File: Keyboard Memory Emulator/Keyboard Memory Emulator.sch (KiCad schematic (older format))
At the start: 38 parts, among them J1 Conn_01x05, J2 Conn_01x01_Male, J3 Conn_01x02, J4 Conn_01x03, J5 Conn_01x02, J6 Conn_01x04, J7 Conn_01x05, J8 Conn_02x05_Odd_Even, SW1 PTS636 SL43 LFS, U1 UPD4168C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

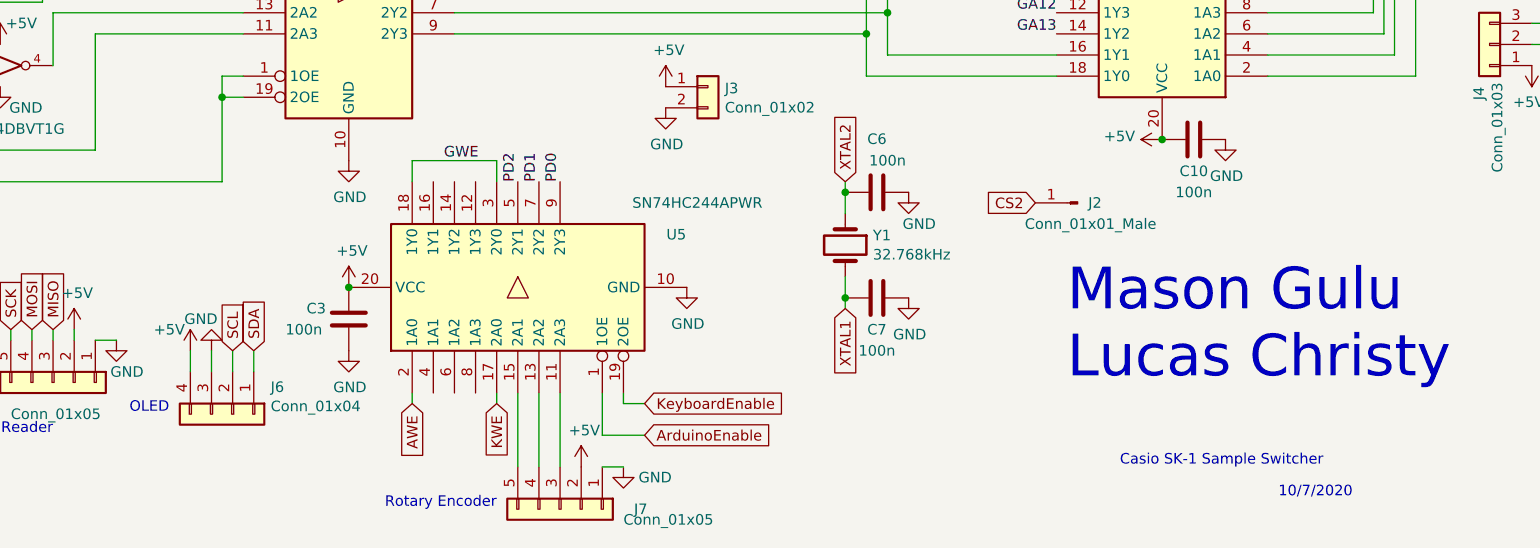
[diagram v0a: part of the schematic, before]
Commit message: Getting closer to finalization
With this update I believe it should be ready to order, waiting to get it looked over beforehand
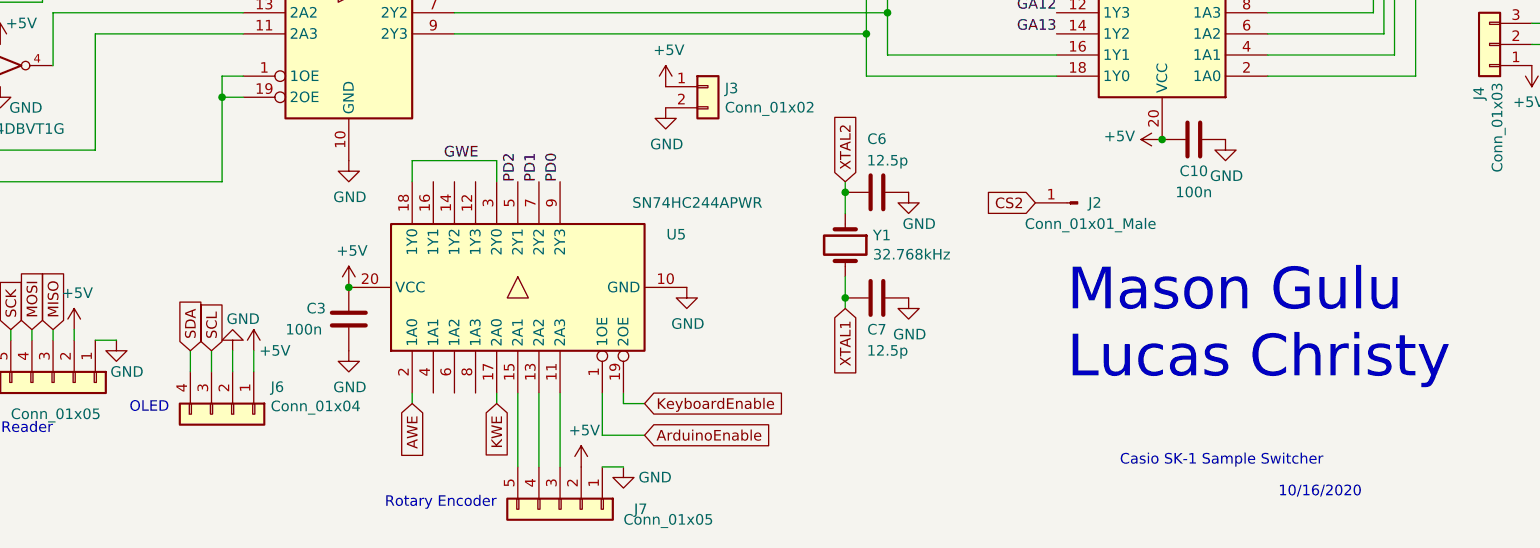
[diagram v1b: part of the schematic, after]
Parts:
- C6, C7: value 100n -> 12.5p
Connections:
- net +5V: now also J6.1 (Pin_1); no longer J6.4 (Pin_4)
- net GND: now also J6.2 (Pin_2); no longer J6.3 (Pin_3)
- net SCL: now also J6.3 (Pin_3); no longer J6.2 (Pin_2)
- net SDA: now also J6.4 (Pin_4); no longer J6.1 (Pin_1)
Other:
- note added: "10/16/2020"
- note removed: "10/7/2020"
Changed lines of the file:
@@
 Casio SK-1 Sample Switcher\n
 Text Notes 8150 7650 0    50   ~ 0
-10/7/2020
+10/16/2020
 Text GLabel 3250 2200 0    50   Input ~ 0
 KeyboardEnable
@@
 	0    1    1    0
 $EndComp
-Text GLabel 3300 6950 1    50   Input ~ 0
+Text GLabel 3000 6950 1    50   Input ~ 0
 SDA
-Text GLabel 3200 6950 1    50   Input ~ 0
+Text GLabel 3100 6950 1    50   Input ~ 0
 SCL
 $Comp
 L power:GND #PWR0136
 U 1 1 5F88AA9C
-P 3100 6950
-F 0 "#PWR0136" H 3100 6700 50  0001 C CNN
+P 3200 6950
+F 0 "#PWR0136" H 3200 6700 50  0001 C CNN
 F 1 "GND" H 3150 6800 50  0000 C CNN
-F 2 "" H 3100 6950 50  0001 C CNN
-F 3 "" H 3100 6950 50  0001 C CNN
-	1    3100 6950
+F 2 "" H 3200 6950 50  0001 C CNN
+F 3 "" H 3200 6950 50  0001 C CNN
+	1    3200 6950
 	-1   0    0    1
 $EndComp
@@
 L power:+5V #PWR0137
 U 1 1 5F88B7D3
-P 3000 6950
-F 0 "#PWR0137" H 3000 6800 50  0001 C CNN
-F 1 "+5V" H 2900 7050 50  0000 C CNN
-F 2 "" H 3000 6950 50  0001 C CNN
-F 3 "" H 3000 6950 50  0001 C CNN
-	1    3000 6950
+P 3300 6950
+F 0 "#PWR0137" H 3300 6800 50  0001 C CNN
+F 1 "+5V" H 3400 6950 50  0000 C CNN
+F 2 "" H 3300 6950 50  0001 C CNN
+F 3 "" H 3300 6950 50  0001 C CNN
+	1    3300 6950
 	1    0    0    -1
 $EndComp
@@
 P 6250 6700
 F 0 "C7" V 6400 6700 50  0000 C CNN
-F 1 "100n" V 6500 6700 50  0000 C CNN
+F 1 "12.5p" V 6500 6750 50  0000 C CNN
 F 2 "Capacitor_THT:C_Disc_D5.1mm_W3.2mm_P5.00mm" H 6288 6550 50  0001 C CNN
 F 3 "~" H 6250 6700 50  0001 C CNN
@@
 P 6250 6200
 F 0 "C6" V 5998 6200 50  0000 C CNN
-F 1 "100n" V 6100 6250 50  0000 C CNN
+F 1 "12.5p" V 6100 6250 50  0000 C CNN
 F 2 "Capacitor_THT:C_Disc_D5.1mm_W3.2mm_P5.00mm" H 6288 6050 50  0001 C CNN
 F 3 "~" H 6250 6200 50  0001 C CNN

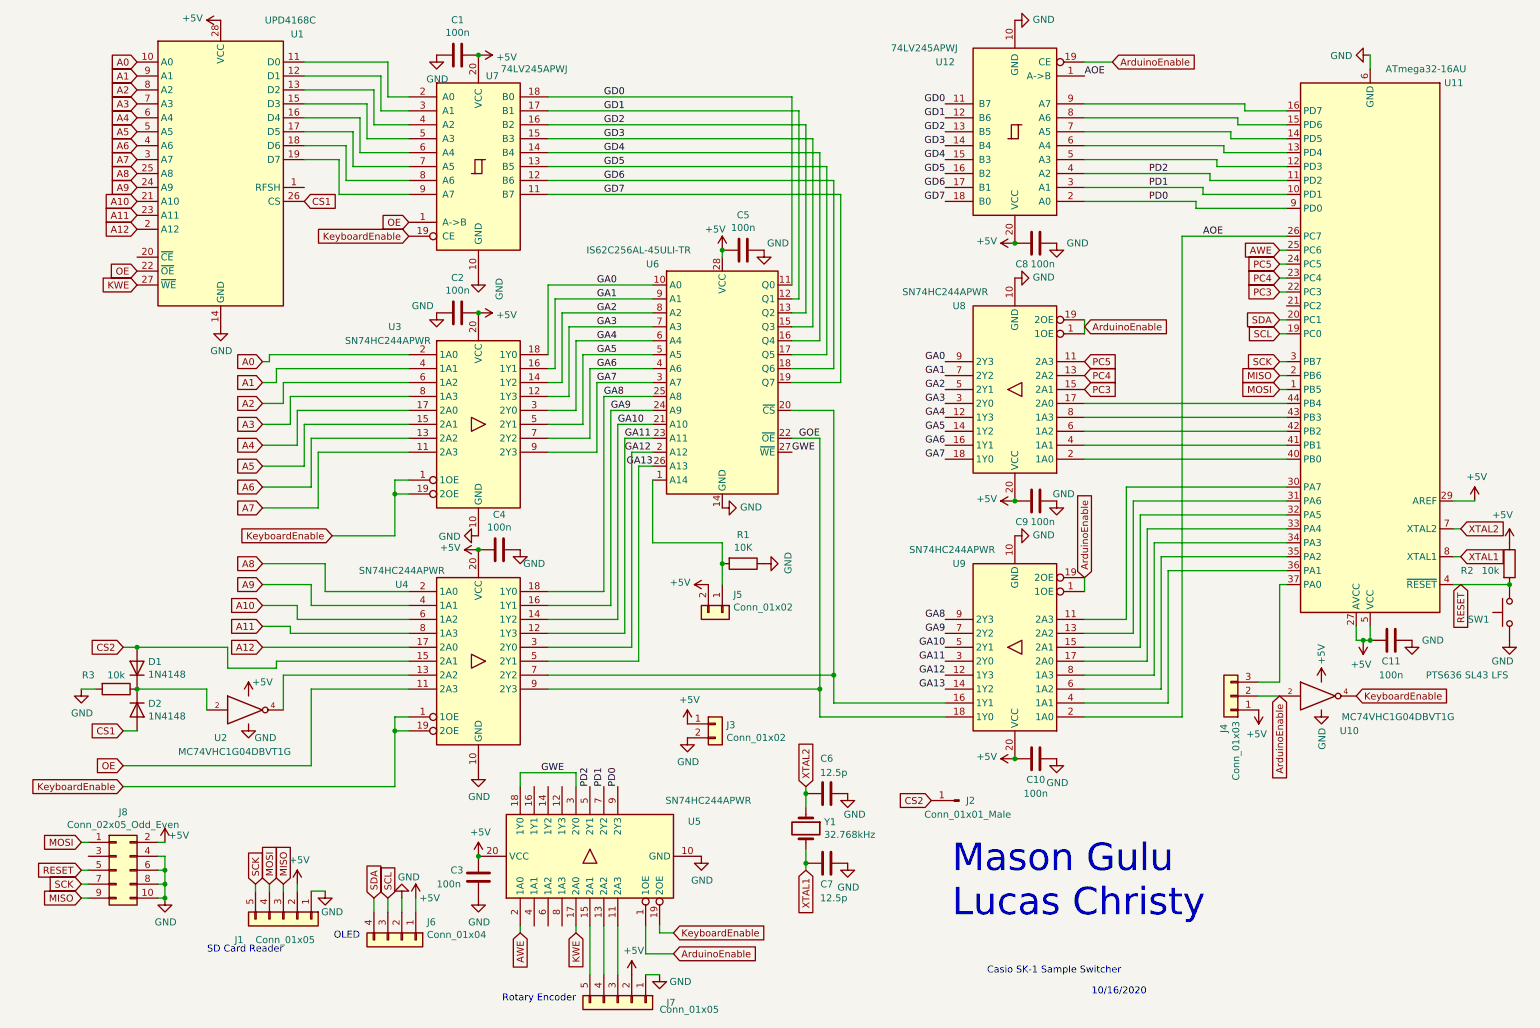
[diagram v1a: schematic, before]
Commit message: Schematic Restructuring to make it cleaner and easier to read. No actual changes as of yet, but planning to add some pull-up resistors on the I2C data bus.
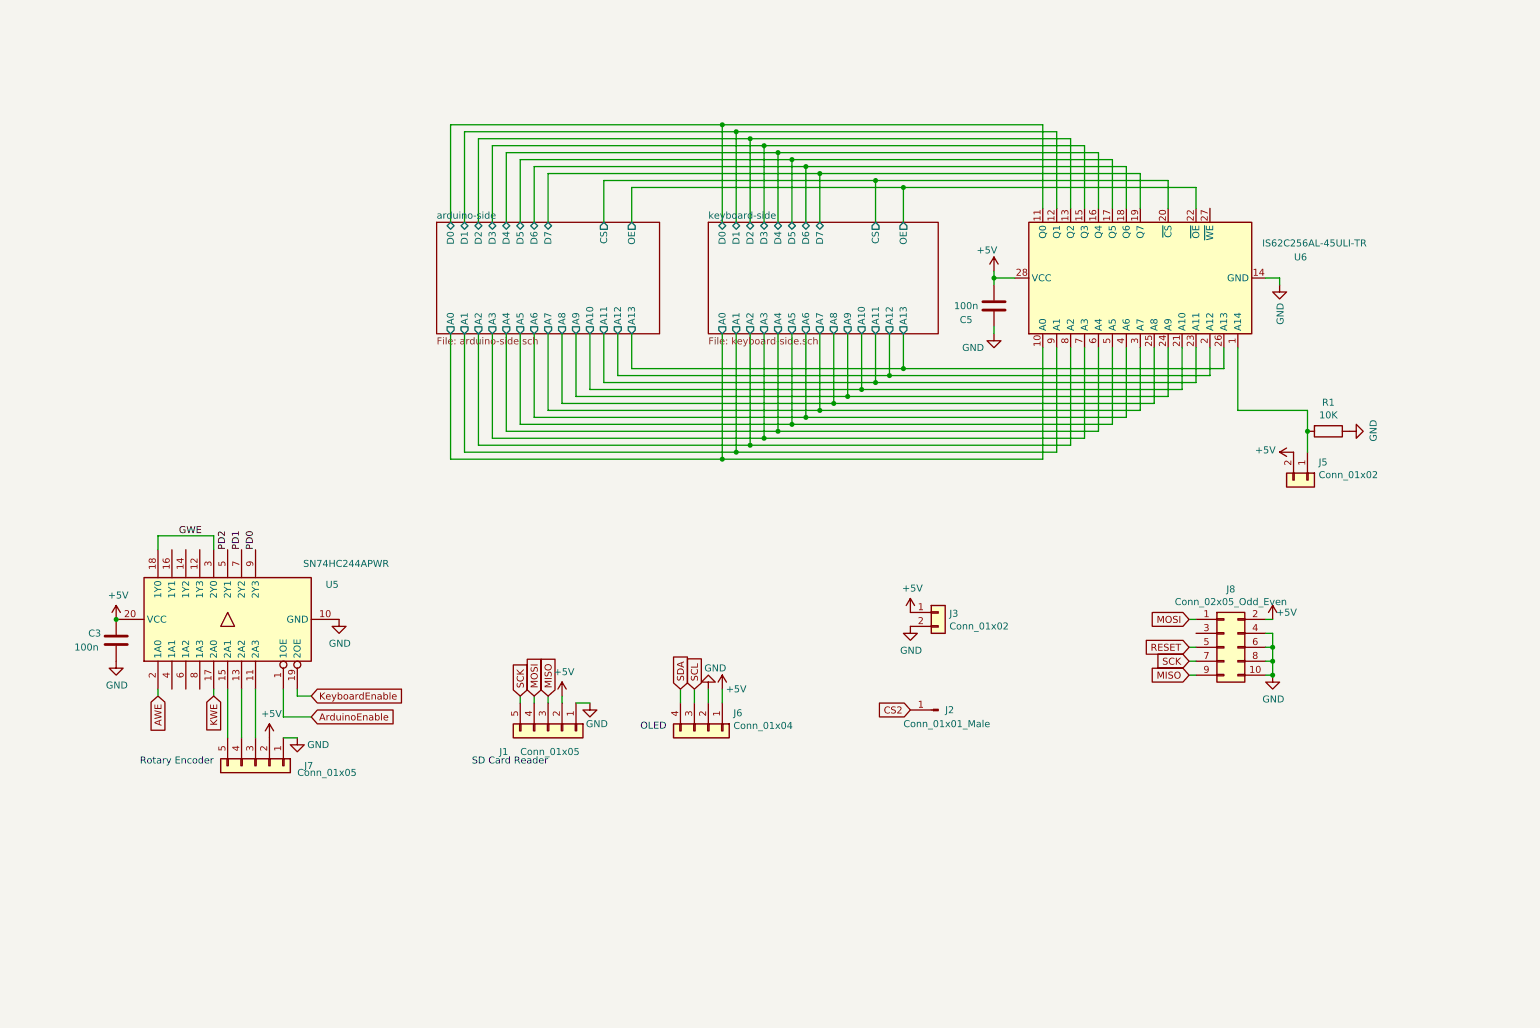
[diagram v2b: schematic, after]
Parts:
- removed C1, C10, C11, C2, C4, C8, C9: 100n, Capacitor_THT:C_Disc_D5.1mm_W3.2mm_P5.00mm, symbol Device:C
- removed C6, C7: 12.5p, Capacitor_THT:C_Disc_D5.1mm_W3.2mm_P5.00mm, symbol Device:C
- removed D1, D2: 1N4148, Diode_THT:D_DO-34_SOD68_P7.62mm_Horizontal, symbol Device:D
- removed J4: Conn_01x03, Connector_PinHeader_2.54mm:PinHeader_1x03_P2.54mm_Vertical, symbol Connector_Generic:Conn_01x03
- removed R2, R3: 10k, Resistor_THT:R_Axial_DIN0204_L3.6mm_D1.6mm_P5.08mm_Horizontal, symbol Device:R
- removed SW1: PTS636 SL43 LFS, Button_Switch_SMD:SW_SPST_REED_CT05-XXXX-G1, symbol Switch:SW_Push
- removed U1: UPD4168C, Package_DIP:DIP-28_W15.24mm, symbol myramchip:UPD4168C
- removed U10, U2: MC74VHC1G04DBVT1G, Package_SO:thispackagefucker, symbol 74xGxx:74AHC1G04
- removed U11: ATmega32-16AU, Package_QFP:TQFP-44_10x10mm_P0.8mm, symbol MCU_Microchip_ATmega:ATmega32-16AU
- removed U12, U7: 74LV245APWJ, Package_SO:TSSOP-20_4.4x6.5mm_P0.65mm, symbol 74xx:74LS245
- removed U3, U4, U8, U9: SN74HC244APWR, Package_SO:TSSOP-20_4.4x6.5mm_P0.65mm, symbol 74xx:74HC244
- removed Y1: 32.768kHz, Crystal:Crystal_C26-LF_D2.1mm_L6.5mm_Horizontal, symbol Device:Crystal
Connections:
- net GWE: no longer U6.27 (~WE)
- net arduino-side/A12: now reaches U6.2 (A12)
- net arduino-side/CS: now reaches U6.20 (~CS)
- net GA0 renamed arduino-side/A0
- net GA1 renamed arduino-side/A1
- net GA10 renamed arduino-side/A10
- net GA11 renamed arduino-side/A11
- net GA13 renamed arduino-side/A13
- net GA2 renamed arduino-side/A2
- net GA3 renamed arduino-side/A3
- net GA4 renamed arduino-side/A4
- net GA5 renamed arduino-side/A5
- net GA6 renamed arduino-side/A6
- net GA7 renamed arduino-side/A7
- net GA8 renamed arduino-side/A8
- net GA9 renamed arduino-side/A9
- net GD0 renamed arduino-side/D0
- net GD1 renamed arduino-side/D1
- net GD2 renamed arduino-side/D2
- net GD3 renamed arduino-side/D3
- net GD4 renamed arduino-side/D4
- net GD5 renamed arduino-side/D5
- net GD6 renamed arduino-side/D6
- net GD7 renamed arduino-side/D7
- net GOE renamed arduino-side/OE
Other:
- note removed: "10/16/2020"
- note removed: "Casio SK-1 Sample Switcher\n"
- note removed: "Mason Gulu\nLucas Christy"
- moved on the sheet: C3, C5, J1, J2, J3, J5, J6, J7, J8, R1, U5, U6

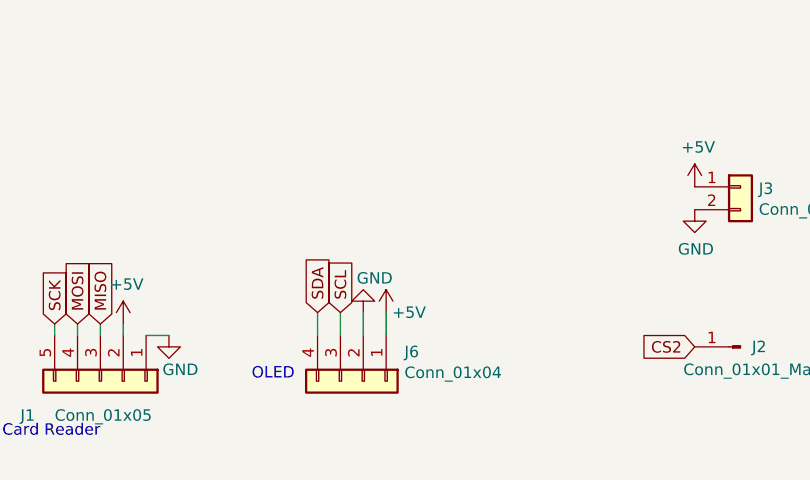
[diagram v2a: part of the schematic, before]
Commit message: Ran the autorouter and updated the PCB
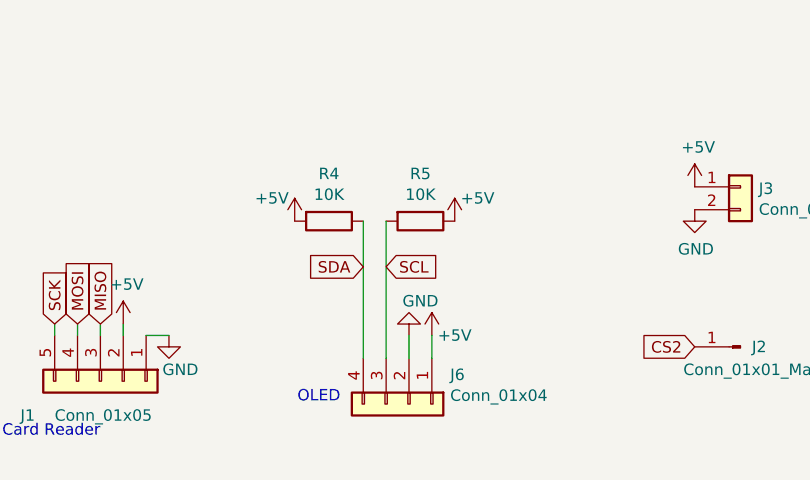
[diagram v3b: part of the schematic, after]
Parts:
- added R4, R5: 10K, Resistor_THT:R_Axial_DIN0204_L3.6mm_D1.6mm_P5.08mm_Horizontal, symbol Device:R
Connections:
- net +5V: now also R4.2, R5.1
- net SCL: now also R5.2
- net SDA: now also R4.1
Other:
- moved on the sheet: J6
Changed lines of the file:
@@
 L Connector_Generic:Conn_01x04 J6
 U 1 1 5F888A84
-P 5400 5750
-F 0 "J6" V 5272 5930 50  0000 L CNN
-F 1 "Conn_01x04" V 5363 5930 50  0000 L CNN
-F 2 "Connector_PinHeader_2.54mm:PinHeader_1x04_P2.54mm_Vertical" H 5400 5750 50  0001 C CNN
-F 3 "~" H 5400 5750 50  0001 C CNN
-	1    5400 5750
+P 5600 5850
+F 0 "J6" V 5472 6030 50  0000 L CNN
+F 1 "Conn_01x04" V 5563 6030 50  0000 L CNN
+F 2 "Connector_PinHeader_2.54mm:PinHeader_1x04_P2.54mm_Vertical" H 5600 5850 50  0001 C CNN
+F 3 "~" H 5600 5850 50  0001 C CNN
+	1    5600 5850
 	0    1    1    0
 $EndComp
-Text GLabel 5200 5450 1    50   Input ~ 0
+Text GLabel 5400 5250 0    50   Input ~ 0
 SDA
-Text GLabel 5300 5450 1    50   Input ~ 0
+Text GLabel 5500 5250 2    50   Input ~ 0
 SCL
 $Comp
 L power:GND #PWR0136
 U 1 1 5F88AA9C
-P 5400 5450
-F 0 "#PWR0136" H 5400 5200 50  0001 C CNN
-F 1 "GND" H 5350 5300 50  0000 C CNN
-F 2 "" H 5400 5450 50  0001 C CNN
-F 3 "" H 5400 5450 50  0001 C CNN
-	1    5400 5450
+P 5600 5550
+F 0 "#PWR0136" H 5600 5300 50  0001 C CNN
+F 1 "GND" H 5550 5400 50  0000 C CNN
+F 2 "" H 5600 5550 50  0001 C CNN
+F 3 "" H 5600 5550 50  0001 C CNN
+	1    5600 5550
 	-1   0    0    1
 $EndComp
@@
 L power:+5V #PWR0137
 U 1 1 5F88B7D3
-P 5500 5450
-F 0 "#PWR0137" H 5500 5300 50  0001 C CNN
-F 1 "+5V" H 5600 5450 50  0000 C CNN
-F 2 "" H 5500 5450 50  0001 C CNN
-F 3 "" H 5500 5450 50  0001 C CNN
-	1    5500 5450
-	1    0    0    -1
-$EndComp
-Wire Wire Line
-	5200 5450 5200 5550
-Wire Wire Line
-	5300 5450 5300 5550
-Wire Wire Line
-	5400 5450 5400 5550
-Wire Wire Line
-	5500 5450 5500 5550
+P 5700 5550
+F 0 "#PWR0137" H 5700 5400 50  0001 C CNN
+F 1 "+5V" H 5800 5550 50  0000 C CNN
+F 2 "" H 5700 5550 50  0001 C CNN
+F 3 "" H 5700 5550 50  0001 C CNN
+	1    5700 5550
+	1    0    0    -1
+$EndComp
+Wire Wire Line
+	5600 5550 5600 5650
+Wire Wire Line
+	5700 5550 5700 5650
 $Comp
 L Connector_Generic:Conn_01x05 J1
@@
 Text Notes 4250 6000 2    50   ~ 0
 SD Card Reader
-Text Notes 5100 5750 2    50   ~ 0
+Text Notes 5300 5850 2    50   ~ 0
 OLED\n
 Text Notes 1850 6000 2    50   ~ 0
@@
 Wire Wire Line
 	5500 3800 7800 3800
+Wire Wire Line
+	5400 5050 5400 5650
+Wire Wire Line
+	5500 5050 5500 5650
+$Comp
+L Device:R R5
+U 1 1 5FD549B2
+P 5650 5050
+F 0 "R5" V 5443 5050 50  0000 C CNN
+F 1 "10K" V 5534 5050 50  0000 C CNN
+F 2 "Resistor_THT:R_Axial_DIN0204_L3.6mm_D1.6mm_P5.08mm_Horizontal" V 5580 5050 50  0001 C CNN
+F 3 "~" H 5650 5050 50  0001 C CNN
+	1    5650 5050
+	0    1    1    0
+$EndComp
+$Comp
+L Device:R R4
+U 1 1 5FD54F08
+P 5250 5050
+F 0 "R4" V 5043 5050 50  0000 C CNN
+F 1 "10K" V 5134 5050 50  0000 C CNN
+F 2 "Resistor_THT:R_Axial_DIN0204_L3.6mm_D1.6mm_P5.08mm_Horizontal" V 5180 5050 50  0001 C CNN
+F 3 "~" H 5250 5050 50  0001 C CNN
+	1    5250 5050
+	0    1    1    0
+$EndComp
+$Comp
+L power:+5V #PWR0150
+U 1 1 5FD55818
+P 5100 5050
+F 0 "#PWR0150" H 5100 4900 50  0001 C CNN
+F 1 "+5V" H 5000 5150 50  0000 C CNN
+F 2 "" H 5100 5050 50  0001 C CNN
+F 3 "" H 5100 5050 50  0001 C CNN
+	1    5100 5050
+	1    0    0    -1
+$EndComp
+$Comp
+L power:+5V #PWR0154
+U 1 1 5FD55C5B
+P 5800 5050
+F 0 "#PWR0154" H 5800 4900 50  0001 C CNN
+F 1 "+5V" H 5900 5150 50  0000 C CNN
+F 2 "" H 5800 5050 50  0001 C CNN
+F 3 "" H 5800 5050 50  0001 C CNN
+	1    5800 5050
+	1    0    0    -1
+$EndComp
 $EndSCHEMATC
